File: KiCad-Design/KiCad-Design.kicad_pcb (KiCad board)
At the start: 2 copper layers, 35 x 35 mm, 68 parts, among them J1 USB_B_Micro, J2 Battery, J3 Ext, J4 OLED, Q1 SI2301, Q2 SI2301, Q3 SI2307CDS-T1-GE3, SW1 MCU BLE Adv, SW2 MCU FLASH, SW3 MCU RESET, U1 PMBT3904, U2 BME280, U3 CP2104, U4 LTC4054ES5-4.2, U5 PMBT3904, U6 PMBT3904, U7 BME680, U8 AP2112K-3.3, U9 ttgo-32-micro-symbols

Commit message: PCB : Initial PCB Design
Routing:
- net GND: track 0.00 -> 271.9 mm, vias 0 -> 1
- net +3V3: track 0.00 -> 102.3 mm, vias 0 -> 5
- net +5V: track 0.00 -> 70.6 mm, vias 0 -> 1
- net MCU_SCL: track 0.00 -> 59.7 mm, vias 0 -> 1
- net +VSW: track 0.00 -> 58.2 mm, vias 0 -> 2
- net MCU_RESET: track 0.00 -> 51.8 mm, vias 0 -> 2
- net MCU_SDA: track 0.00 -> 45.2 mm, vias 0 -> 2
- net MCU_FLASH: track 0.00 -> 30.8 mm, vias 0 -> 2
- net +BATT: track 0.00 -> 26.8 mm, vias 0 -> 1
- net Net-(Q1-Pad1): track 0.00 -> 18.7 mm
- net MCU_BLE_Adv: track 0.00 -> 18.0 mm, vias 0 -> 1
- net VCC: track 0.00 -> 17.7 mm, vias 0 -> 1
- net Net-(R15-Pad1): track 0.00 -> 13.9 mm, vias 0 -> 1
- net Net-(J1-Pad6): track 0.00 -> 13.3 mm
- net Net-(C2-Pad2): track 0.00 -> 13.0 mm, vias 0 -> 1
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
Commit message: PCB : Finalizing the PCB v1
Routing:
- net GND: track 271.9 -> 398.5 mm
- net +VSW: track 58.2 -> 105.6 mm
- net +5V: track 70.6 -> 114.2 mm
- net +3V3: track 102.3 -> 123.6 mm
- net +BATT: track 26.8 -> 46.8 mm
- net MCU_BAT_REF: track 8.49 -> 15.5 mm
- added copper zone on B.Cu, net GND
- added copper zone on F.Cu, net GND

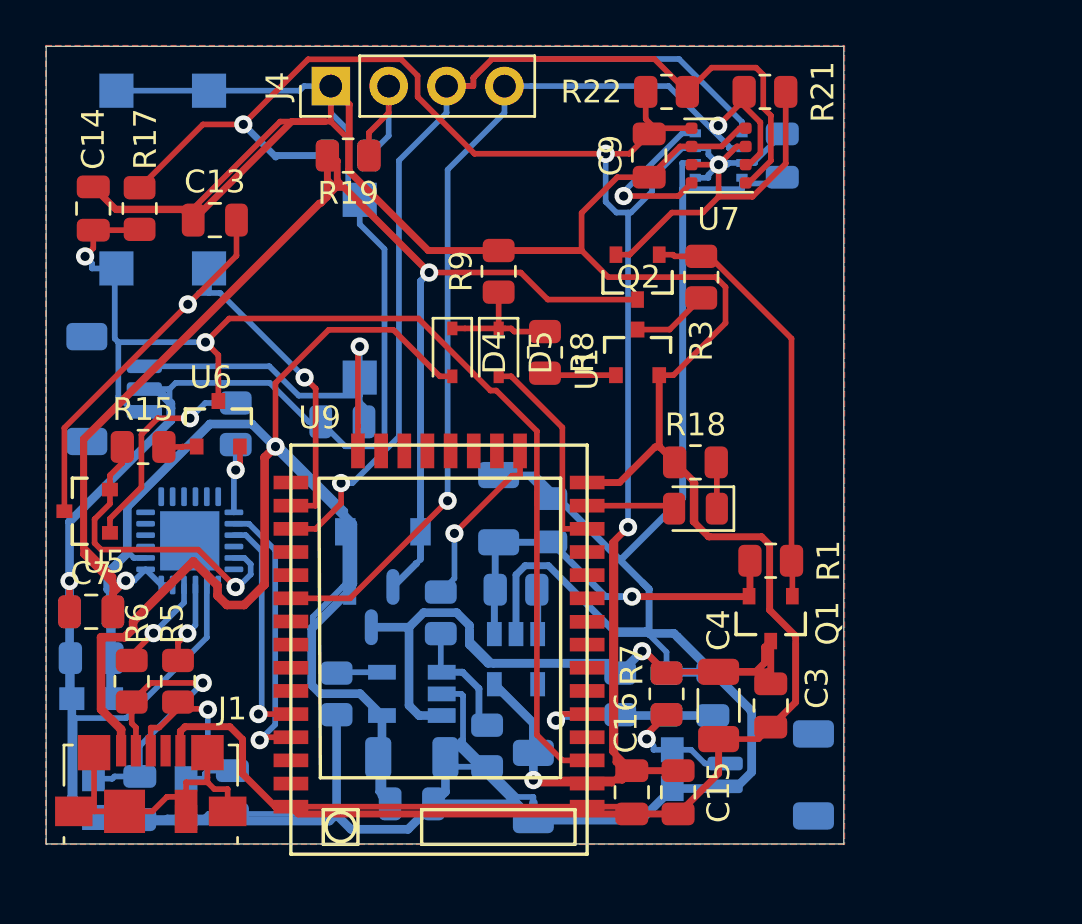
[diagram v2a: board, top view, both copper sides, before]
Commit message: PCB : Adjusting the labels on the PCB file
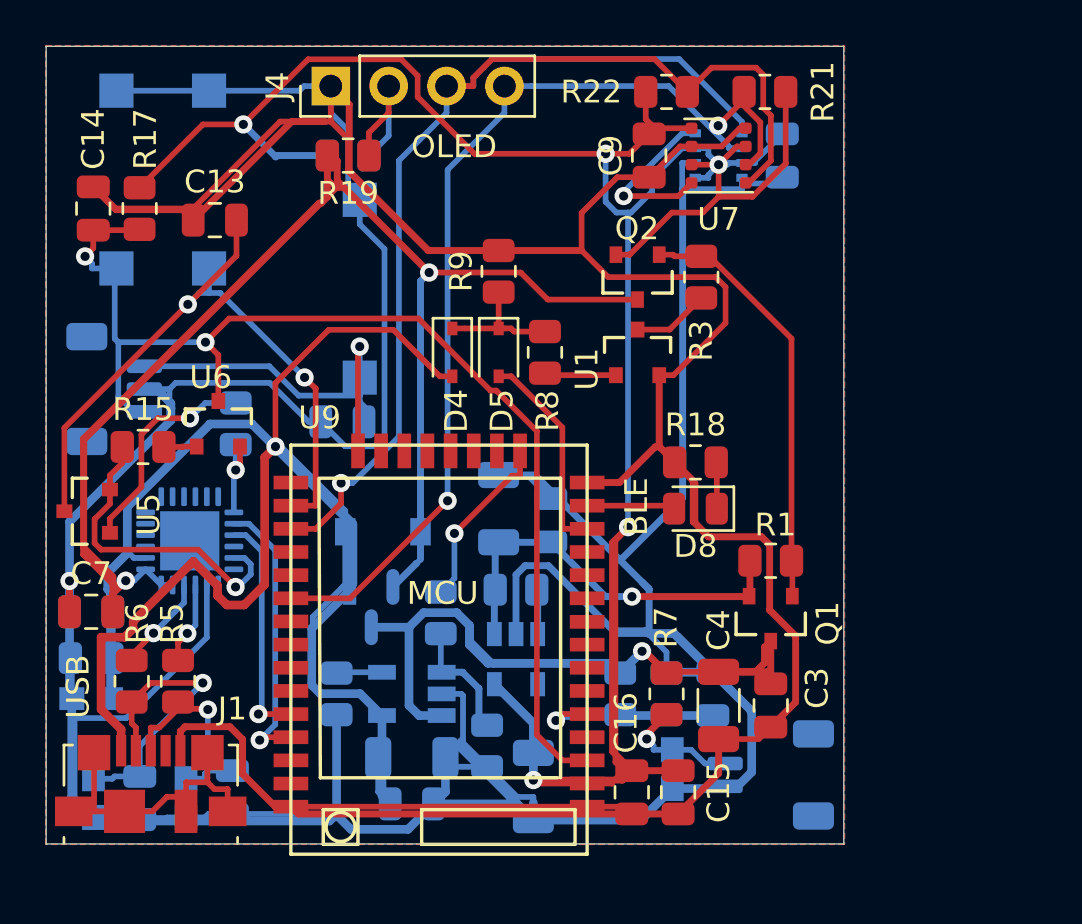
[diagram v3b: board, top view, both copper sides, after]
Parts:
- renumbered SW1 to BLE, SW2 to FLASH, SW3 to RESET
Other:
- board text added: "BATT"
- board text added: "BLE"
- board text added: "Ext"
- board text added: "MCU"
- board text added: "OLED"
- board text added: "USB"
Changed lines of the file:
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@@
   (general
     (thickness 1.6)
-    (drawings 4)
+    (drawings 10)
     (tracks 728)
     (zones 0)
@@
   )
   (setup
-    (last_trace_width 0.3048)
+    (last_trace_width 0.25)
     (user_trace_width 0.254)
     (user_trace_width 0.3048)
@@
     (tags capacitor)
     (attr smd)
-    (fp_text reference C1 (at 0 1.68 90) (layer B.SilkS)
+    (fp_text reference C1 (at 2.816 -0.154 90) (layer B.SilkS)
       (effects (font (size 1 1) (thickness 0.15)) (justify mirror))
     )
@@
     (tags capacitor)
     (attr smd)
-    (fp_text reference C10 (at 0 1.68) (layer B.SilkS)
+    (fp_text reference C10 (at -2.946 0.058) (layer B.SilkS)
       (effects (font (size 1 1) (thickness 0.15)) (justify mirror))
     )
@@
     (tags capacitor)
     (attr smd)
-    (fp_text reference C11 (at 0 1.85) (layer B.SilkS)
+    (fp_text reference C11 (at -3.646 -0.01) (layer B.SilkS)
       (effects (font (size 1 1) (thickness 0.15)) (justify mirror))
     )
@@
     (tags capacitor)
     (attr smd)
-    (fp_text reference C18 (at 0 -1.778 90) (layer B.SilkS)
+    (fp_text reference C18 (at -3.896 -0.058 90) (layer B.SilkS)
       (effects (font (size 1 1) (thickness 0.15)) (justify mirror))
     )
@@
     (tags capacitor)
     (attr smd)
-    (fp_text reference C19 (at -0.254 -2.032 90) (layer B.SilkS)
+    (fp_text reference C19 (at 3.688 0.044 90) (layer B.SilkS)
       (effects (font (size 1 1) (thickness 0.15)) (justify mirror))
     )
@@
     (tags SOD-323)
     (attr smd)
-    (fp_text reference D4 (at 0 -1.85 90) (layer F.SilkS)
+    (fp_text reference D4 (at 2.57 -0.176 90) (layer F.SilkS)
       (effects (font (size 1 1) (thickness 0.15)))
     )
@@
     (tags SOD-323)
     (attr smd)
-    (fp_text reference D5 (at 0 -1.85 90) (layer F.SilkS)
+    (fp_text reference D5 (at 2.57 -0.144 90) (layer F.SilkS)
       (effects (font (size 1 1) (thickness 0.15)))
     )
@@
     (tags LED)
     (attr smd)
-    (fp_text reference D8 (at 0 -1.65) (layer F.SilkS) hide
-      (effects (font (size 1 1) (thickness 0.15)))
-    )
-    (fp_text value LED (at 0 -1.778) (layer F.Fab)
+    (fp_text reference D8 (at 0 -1.65) (layer F.SilkS)
+      (effects (font (size 1 1) (thickness 0.15)))
+    )
+    (fp_text value LED (at 0 -1.778) (layer F.Fab) hide
       (effects (font (size 1 1) (thickness 0.15)))
     )
@@
     (tags "connector JST SH top entry")
     (attr smd)
-    (fp_text reference J2 (at 0 3.98 270) (layer B.SilkS)
+    (fp_text reference J2 (at -0.172 -0.106 270) (layer B.SilkS)
       (effects (font (size 1 1) (thickness 0.15)) (justify mirror))
     )
@@
     (tags "connector JST SH side entry")
     (attr smd)
-    (fp_text reference J3 (at 0 3.3 90) (layer B.SilkS)
+    (fp_text reference J3 (at 0.16 0.184 90) (layer B.SilkS)
       (effects (font (size 1 1) (thickness 0.15)) (justify mirror))
     )
@@
   (module SI2301:Vishay-S-03946-07_2001-K-0 (layer F.Cu)
     (at 250.952 135.128 180)
-    (fp_text reference Q2 (at -1.016 0) (layer F.SilkS)
+    (fp_text reference Q2 (at -0.948 2.128) (layer F.SilkS)
       (effects (font (size 1 1) (thickness 0.15)) (justify right))
     )
@@
   (module SI2307:Vishay-S-03946-07_2001-K-IPC_B (layer B.Cu)
     (at 239.268 149.606 270)
-    (fp_text reference Q3 (at -2.172304 2.66 90) (layer B.SilkS)
+    (fp_text reference Q3 (at -1.206 2.368 90) (layer B.SilkS)
       (effects (font (size 1 1) (thickness 0.15)) (justify left mirror))
     )
@@
     (tags resistor)
     (attr smd)
-    (fp_text reference R1 (at -2.54 0 90) (layer F.SilkS)
+    (fp_text reference R1 (at -0.206 1.574 180) (layer F.SilkS)
       (effects (font (size 1 1) (thickness 0.15)))
     )
@@
     (tags resistor)
     (attr smd)
-    (fp_text reference R2 (at 0 1.65 90) (layer B.SilkS)
+    (fp_text reference R2 (at 2.616 0.178 90) (layer B.SilkS)
       (effects (font (size 1 1) (thickness 0.15)) (justify mirror))
     )
@@
     (tags resistor)
     (attr smd)
-    (fp_text reference R4 (at 0 1.65 90) (layer B.SilkS)
+    (fp_text reference R4 (at 2.416 0.01 90) (layer B.SilkS)
       (effects (font (size 1 1) (thickness 0.15)) (justify mirror))
     )
@@
     (tags resistor)
     (attr smd)
-    (fp_text reference R7 (at 1.27 -1.524 90) (layer F.SilkS)
+    (fp_text reference R7 (at 2.916 -0.022 90) (layer F.SilkS)
       (effects (font (size 1 1) (thickness 0.15)))
     )
@@
     (tags resistor)
     (attr smd)
-    (fp_text reference R8 (at 0 -1.65 90) (layer F.SilkS)
+    (fp_text reference R8 (at 2.57 -0.112 90) (layer F.SilkS)
       (effects (font (size 1 1) (thickness 0.15)))
     )
@@
     (tags resistor)
     (attr smd)
-    (fp_text reference R11 (at 1.27 -1.778 90) (layer B.SilkS)
+    (fp_text reference R11 (at 0.96 1.484 90) (layer B.SilkS)
       (effects (font (size 1 1) (thickness 0.15)) (justify mirror))
     )
@@
     (tags resistor)
     (attr smd)
-    (fp_text reference R12 (at -3.048 0 270) (layer B.SilkS)
+    (fp_text reference R12 (at -2.698 0 270) (layer B.SilkS)
       (effects (font (size 1 1) (thickness 0.15)) (justify mirror))
     )
@@
     (tags resistor)
     (attr smd)
-    (fp_text reference R13 (at 3.048 -0.254 90) (layer B.SilkS)
+    (fp_text reference R13 (at 0.016 -1.844 90) (layer B.SilkS)
       (effects (font (size 1 1) (thickness 0.15)) (justify mirror))
     )
@@
     (tags resistor)
     (attr smd)
-    (fp_text reference R14 (at 0 1.65 270) (layer B.SilkS)
+    (fp_text reference R14 (at 2.864 -0.018 270) (layer B.SilkS)
       (effects (font (size 1 1) (thickness 0.15)) (justify mirror))
     )
@@
     (tags resistor)
     (attr smd)
-    (fp_text reference R16 (at -3.556 0) (layer B.SilkS)
+    (fp_text reference R16 (at -3.182 0) (layer B.SilkS)
       (effects (font (size 1 1) (thickness 0.15)) (justify mirror))
     )
@@
     (tags resistor)
     (attr smd)
-    (fp_text reference R20 (at 0 -1.778) (layer B.SilkS)
+    (fp_text reference R20 (at -4.448 -0.006) (layer B.SilkS)
       (effects (font (size 1 1) (thickness 0.15)) (justify mirror))
     )
@@
     (tags "SPST button tactile switch")
     (attr smd)
-    (fp_text reference SW1 (at 0 2.6 270) (layer B.SilkS)
+    (fp_text reference BLE (at 0 2.6 270) (layer B.SilkS)
       (effects (font (size 1 1) (thickness 0.15)) (justify mirror))
     )
@@
     (tags "SPST button tactile switch")
     (attr smd)
-    (fp_text reference SW2 (at 0 2.6 90) (layer B.SilkS)
+    (fp_text reference FLASH (at 0 2.6 90) (layer B.SilkS)
       (effects (font (size 1 1) (thickness 0.15)) (justify mirror))
     )
@@
     (tags "SPST button tactile switch")
     (attr smd)
-    (fp_text reference SW3 (at 0 2.6 -90) (layer B.SilkS)
+    (fp_text reference RESET (at -5.652 0.016) (layer B.SilkS)
       (effects (font (size 1 1) (thickness 0.15)) (justify mirror))
     )
@@
   (module PMBT3904:NXP-PMBT3904,215-0 (layer F.Cu)
     (at 226.8 145.4 180)
-    (fp_text reference U5 (at -1.675 -2.225) (layer F.SilkS)
+    (fp_text reference U5 (at -2.7 0.8 90) (layer F.SilkS)
       (effects (font (size 1 1) (thickness 0.15)) (justify right))
     )
@@
     (tags SOT-23-5)
     (attr smd)
-    (fp_text reference U8 (at 0 -3.048 90) (layer B.SilkS)
+    (fp_text reference U8 (at 0 -2.682 90) (layer B.SilkS)
       (effects (font (size 1 1) (thickness 0.15)) (justify mirror))
     )
@@
     )
   )
+  (gr_text BLE (at 250.9 145.2 90) (layer F.SilkS)
+    (effects (font (size 1 1) (thickness 0.15)))
+  )
+  (gr_text MCU (at 242.4 149) (layer F.SilkS)
+    (effects (font (size 1 1) (thickness 0.15)))
+  )
+  (gr_text USB (at 226.4 153.1 90) (layer F.SilkS)
+    (effects (font (size 1 1) (thickness 0.15)))
+  )
+  (gr_text OLED (at 242.9 129.4) (layer F.SilkS)
+    (effects (font (size 1 1) (thickness 0.15)))
+  )
+  (gr_text Ext (at 230.9 140.6 90) (layer B.SilkS)
+    (effects (font (size 1 1) (thickness 0.15)) (justify mirror))
+  )
+  (gr_text BATT (at 257.7 153.7) (layer B.SilkS)
+    (effects (font (size 1 1) (thickness 0.15)) (justify mirror))
+  )
   (gr_line (start 260 125) (end 260 160) (layer Edge.Cuts) (width 0.05))

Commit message: PCB : Adding HDC1080 in the design
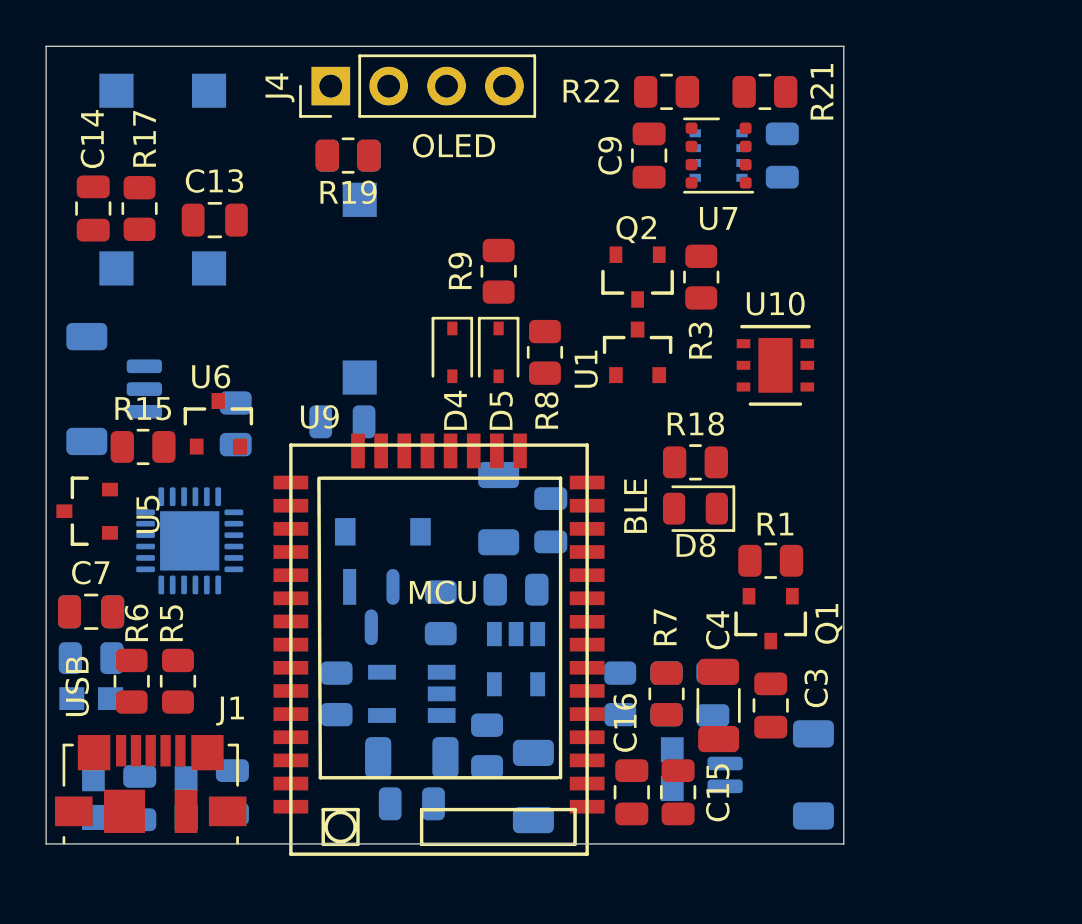
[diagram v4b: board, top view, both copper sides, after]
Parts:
- added U10: HDC1080, Package_SON:Texas_PWSON-N6, F.Cu at (257.0, 139.0)
- renumbered BLE to SW1, FLASH to SW2, RESET to SW3
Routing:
- net GND: track 398.5 -> 0.00 mm, vias 1 -> 0
- net +3V3: track 123.6 -> 0.00 mm, vias 5 -> 0
- net +5V: track 114.2 -> 0.00 mm, vias 1 -> 0
- net +VSW: track 105.6 -> 0.00 mm, vias 2 -> 0
- net MCU_SCL: track 59.7 -> 0.00 mm, vias 1 -> 0
- net MCU_RESET: track 51.8 -> 0.00 mm, vias 2 -> 0
- net +BATT: track 46.8 -> 0.00 mm, vias 1 -> 0
- net MCU_SDA: track 45.2 -> 0.00 mm, vias 2 -> 0
- net MCU_FLASH: track 30.8 -> 0.00 mm, vias 2 -> 0
- net Net-(Q1-Pad1): track 18.7 -> 0.00 mm
- net MCU_BLE_Adv: track 18.0 -> 0.00 mm, vias 1 -> 0
- net VCC: track 17.7 -> 0.00 mm, vias 1 -> 0
- net MCU_BAT_REF: track 15.5 -> 0.00 mm, vias 1 -> 0
- net Net-(R15-Pad1): track 13.9 -> 0.00 mm, vias 1 -> 0
- net Net-(J1-Pad6): track 13.3 -> 0.00 mm
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- removed copper zone on B.Cu, net GND
- removed copper zone on F.Cu, net GND

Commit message: PCB : Using UMH3N package instead of PMBT3904
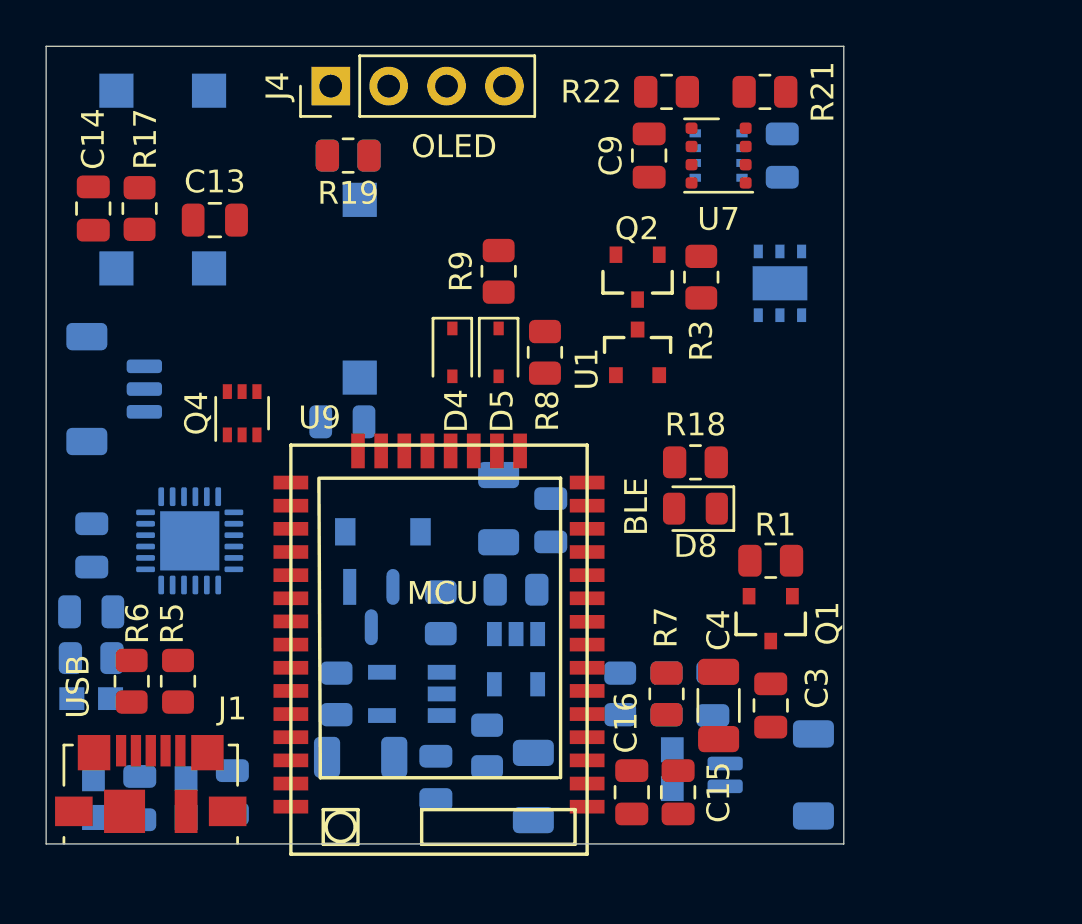
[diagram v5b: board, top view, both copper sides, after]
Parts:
- removed R14, R15: 10K, Resistor_SMD:R_0805_2012Metric
- removed U5, U6: PMBT3904, PMBT3904:NXP-PMBT3904,215-0
- added Q4: UMH3N, Package_TO_SOT_SMD:SOT-363_SC-70-6, F.Cu at (233.6, 141.1)
- C7, U10: moved to B.Cu
- moved U10 3.61 mm to (257.2, 135.4), turned to 270 degrees
- moved C7 2.91 mm to (227.0, 146.9), turned to 270 degrees
- moved C11 2.25 mm to (238.8, 156.2), turned to 180 degrees
- moved C10 1.55 mm to (242.1, 157.1), turned to 270 degrees

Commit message: PCB: Updating the PCB design file :)
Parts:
- removed R21, R22: 4.7K, Resistor_SMD:R_0805_2012Metric
- removed U10: HDC1080, Package_SON:Texas_PWSON-N6
- removed the U7 at (254.5, 129.8)
- added C10: 100nF, Capacitor_SMD:C_0805_2012Metric, B.Cu at (264.5, 140.9)
- added J3: SENSOR, Connector_PinHeader_1.27mm:PinHeader_1x04_P1.27mm_Vertical, F.Cu at (262.5, 147.5)
- added J5: SENSORS, Connector_JST:JST_SH_BM04B-SRSS-TB_1x04-1MP_P1.00mm_Vertical, F.Cu at (257.2, 136.8)
- added R14: 4.7K, Resistor_SMD:R_0805_2012Metric, B.Cu at (266.1, 144.7)
- added R15: 4.7K, Resistor_SMD:R_0805_2012Metric, B.Cu at (262.8, 144.7)
- added U5: HDC1080, Package_SON:Texas_PWSON-N6, F.Cu at (264.3, 130.1)
- added U6: BME680, Package_LGA:Bosch_LGA-8_3x3mm_P0.8mm_ClockwisePinNumbering, F.Cu at (264.5, 140.8)
- C14: renamed from C13; moved to B.Cu
- C16: renamed from C15; moved to B.Cu
- C9, D4, D5, R8, R9: moved to B.Cu
- D3, J2, SW1, SW2, SW3, U2: moved to F.Cu
- J4: renamed from J3; moved to F.Cu
- moved Q4 17.2 mm to (232.5, 133.8), turned to 0 degrees
- moved C9 15.1 mm to (264.5, 137.5), turned to 0 degrees
- moved C13 15.0 mm to (250.1, 132.7), turned to 180 degrees
- moved U2 12.6 mm to (264.5, 137.4), turned to 270 degrees
- moved SW2 11.5 mm to (242.1, 136.6), turned to 270 degrees
- moved SW3 11.3 mm to (237.8, 136.6), turned to 270 degrees
- moved R19 11.0 mm to (228.1, 134.0), turned to 270 degrees
- moved R20 11.0 mm to (228.1, 134.0), turned to 270 degrees
- moved C14 9.84 mm to (242.0, 134.8), turned to 180 degrees
- moved SW1 7.60 mm to (246.3, 136.6), turned to 270 degrees
- moved C8 7.01 mm to (264.3, 130.2), turned to 180 degrees
- moved C15 4.39 mm to (231.1, 133.9)
- moved R17 4.39 mm to (233.1, 133.9)
- moved C4 3.97 mm to (252.5, 150.5), turned to 0 degrees
- moved J6 2.62 mm to (238.4, 129.2)
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- renumbered C10 to C11, C11 to C12, C12 to C13, C14 to C15, C16 to C17, C17 to C18, C18 to C19, C19 to C20, J4 to J6, Q4 to Q3, Q3 to Q4, U8 to U7, U9 to U8
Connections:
- C8 pad 1: GND -> SEN_VCC
- C8 pad 2: +3V3 -> SEN_GND
- C9 pad 1: GND -> SEN_VCC
- C9 pad 2: +3V3 -> SEN_GND
- U2 pad 1: GND -> SEN_GND
- U2 pad 2: +3V3 -> Net-(U2-Pad2)
- U2 pad 3: MCU_SDA -> SEN_SDA
- U2 pad 4: MCU_SCL -> SEN_SCL
- U2 pad 6: +3V3 -> SEN_VCC
- U2 pad 7: GND -> SEN_GND
- U2 pad 8: +3V3 -> SEN_VCC
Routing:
- net GND: track 0.00 -> 402.2 mm, vias 0 -> 1
- net +3V3: track 0.00 -> 113.6 mm, vias 0 -> 2
- net +5V: track 0.00 -> 102.4 mm, vias 0 -> 1
- net +VSW: track 0.00 -> 89.4 mm, vias 0 -> 2
- net SEN_VCC: track 0.00 -> 73.2 mm
- net +BATT: track 0.00 -> 71.2 mm, vias 0 -> 1
- net MCU_BLE_Adv: track 0.00 -> 66.0 mm, vias 0 -> 2
- net SEN_GND: track 0.00 -> 62.4 mm, vias 0 -> 2
- net MCU_RESET: track 0.00 -> 45.5 mm, vias 0 -> 2
- net MCU_SDA: track 0.00 -> 45.3 mm, vias 0 -> 1
- net MCU_SCL: track 0.00 -> 38.0 mm
- net VCC: track 0.00 -> 35.1 mm, vias 0 -> 1
- net Net-(J6-Pad2): track 0.00 -> 34.8 mm
- net SEN_SCL: track 0.00 -> 31.9 mm, vias 0 -> 1
- net MCU_FLASH: track 0.00 -> 31.0 mm, vias 0 -> 1
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- added copper zone on B.Cu, net GND
- added copper zone on F.Cu, net GND
- added copper zone on B.Cu, net SEN_GND
- added copper zone on F.Cu, net SEN_GND
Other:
- board size 35 x 35 mm -> 43.3 x 33 mm
- board text removed: "BATT"
- board text removed: "Ext"

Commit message: MISC: Committing some left overs
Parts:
- renumbered J2 to BAT, SW1 to BLE, U2 to BME280, U6 to BME680, J3 to BUS, U8 to ESP32, J4 to External, SW2 to FLASH, U5 to HDC1080, J6 to OLED, SW3 to RST, J5 to Sensors
